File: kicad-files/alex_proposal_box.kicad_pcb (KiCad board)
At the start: 2 copper layers, 69 x 69 mm, 40 parts, among them J1 Conn_01x06_Pin, J2 Conn_01x06_Socket, Q1 2N7000, Q10 2N7000, Q11 2N7000, Q2 2N7000, Q3 2N7000, Q4 2N7000, Q5 2N7000, Q6 2N7000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

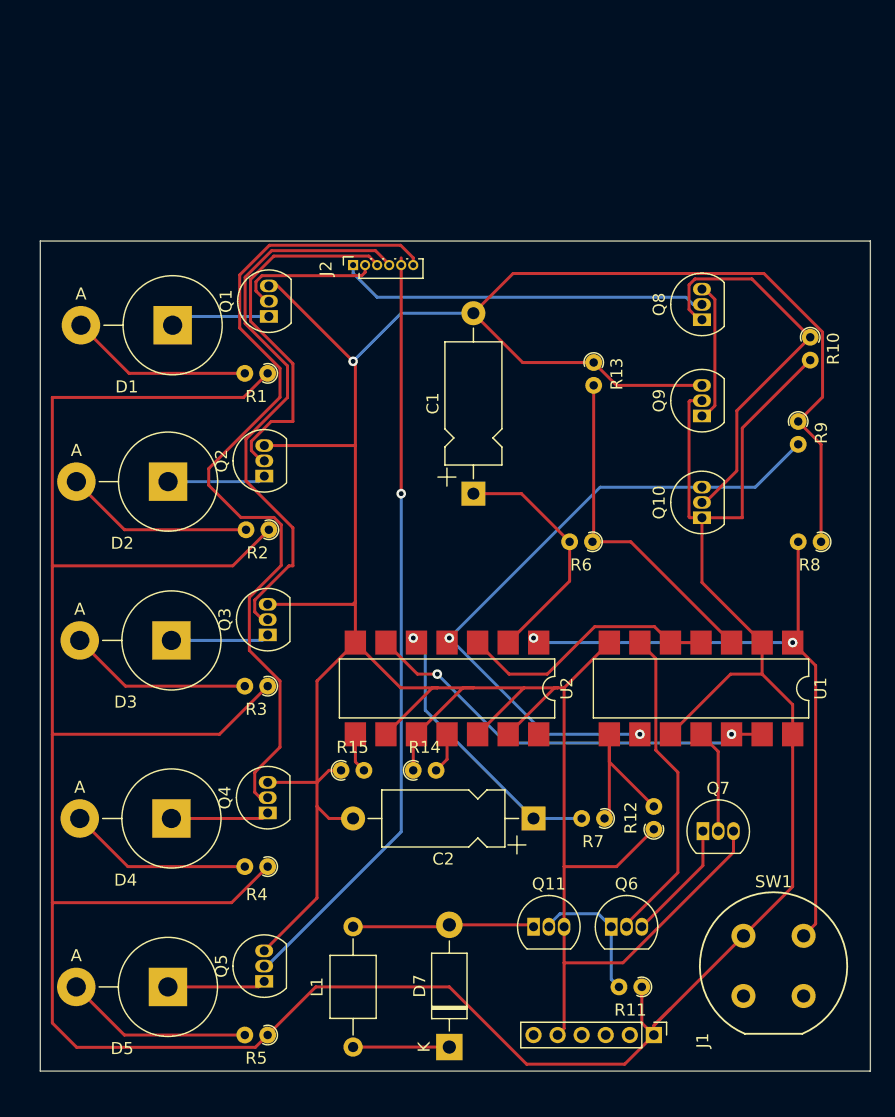
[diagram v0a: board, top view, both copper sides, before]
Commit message: made the schematic printable on a PCB
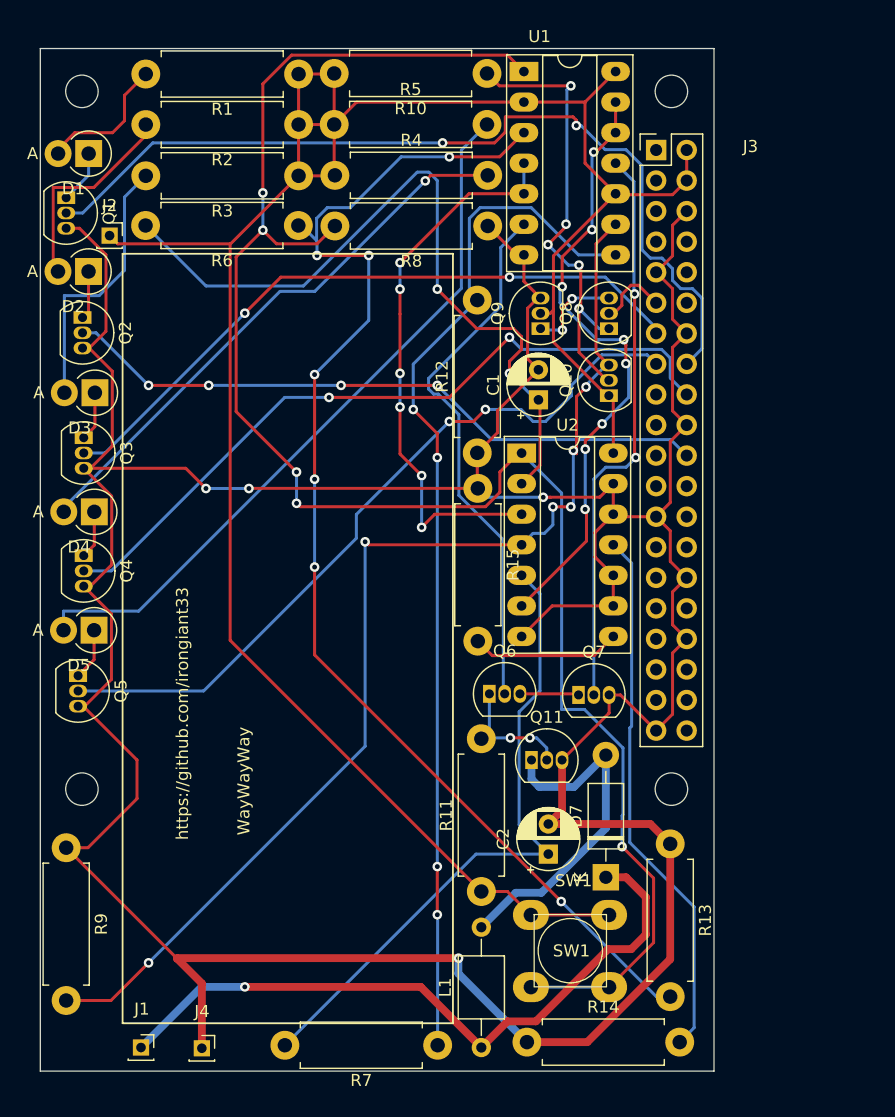
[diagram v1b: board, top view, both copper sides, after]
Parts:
- added J3: Conn_02x20_Odd_Even, Connector_PinHeader_2.54mm:PinHeader_2x20_P2.54mm_Vertical, F.Cu at (143.2, 57.4)
- added J4: Conn_01x01_Socket, Connector_PinSocket_2.00mm:PinSocket_1x01_P2.00mm_Vertical, F.Cu at (105.4, 132.1)
- added REF**: MountingHole_2.7mm, MountingHole:MountingHole_2.7mm, F.Cu at (144.5, 110.6)
- added REF**: MountingHole_2.7mm, MountingHole:MountingHole_2.7mm, F.Cu at (95.5, 52.6)
- added REF**: MountingHole_2.7mm, MountingHole:MountingHole_2.7mm, F.Cu at (144.5, 52.6)
- added REF**: MountingHole_2.7mm, MountingHole:MountingHole_2.7mm, F.Cu at (95.5, 110.6)
- C1, C2: footprint Capacitor_THT:CP_Axial_L10.0mm_D4.5mm_P15.00mm_Horizontal -> Capacitor_THT:CP_Radial_D5.0mm_P2.50mm
- D1, D2, D3, D4, D5: footprint Diode_THT:D_5KPW_P7.62mm_Vertical_AnodeUp -> Diode_THT:D_DO-15_P2.54mm_Vertical_AnodeUp
- J1: value Conn_01x06_Pin -> Conn_01x01_Socket; footprint Connector_PinHeader_2.00mm:PinHeader_1x06_P2.00mm_Vertical -> Connector_PinSocket_2.00mm:PinSocket_1x01_P2.00mm_Vertical
- J2: value Conn_01x06_Socket -> Conn_01x01_Socket; footprint Connector_PinSocket_1.00mm:PinSocket_1x06_P1.00mm_Vertical -> Connector_PinSocket_2.00mm:PinSocket_1x01_P2.00mm_Vertical
- R1, R10, R11, R12, R13, R14, R15, R2, R3, R4, R5, R6, R7, R8, R9: footprint Resistor_THT:R_Axial_DIN0204_L3.6mm_D1.6mm_P1.90mm_Vertical -> Resistor_THT:R_Axial_DIN0411_L9.9mm_D3.6mm_P12.70mm_Horizontal
- SW1: footprint Button_Switch_THT:Push_E-Switch_KS01Q01 -> SamsFootprints:SW_PUSH-6.5mm
- U1, U2: footprint Package_DIP:SMDIP-14_W7.62mm -> Package_DIP:DIP-14_W7.62mm_Socket_LongPads
- moved R5 75.9 mm to (116.4, 55.3), turned to 0 degrees
- moved R9 70.4 mm to (94.2, 115.4)
- moved R4 57.7 mm to (116.5, 59.5), turned to 0 degrees
- moved U1 53.4 mm to (132.2, 50.9), turned to 0 degrees
- moved J1 42.6 mm to (100.4, 132.0), turned to 0 degrees
- moved R3 42.5 mm to (113.5, 59.6)
- moved R13 40.5 mm to (144.4, 115.1)
- moved R8 38.2 mm to (129.2, 63.8)
- moved R6 35.9 mm to (113.5, 63.7)
- moved R10 34.7 mm to (129.1, 51.1), turned to 180 degrees
- moved R12 34.6 mm to (128.3, 82.6)
- moved R2 33.8 mm to (113.5, 55.3)
- moved D5 30.3 mm to (96.5, 97.3)
- moved Q5 29.7 mm to (95.1, 101.1), turned to -90 degrees
- moved Q4 26.3 mm to (95.6, 91.2), turned to -90 degrees
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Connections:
- J1 pad 1: +5VD -> +12V
- J2 pad 1: Net-(J2-Pin_1) -> +5VD
- Q1 pad 2: Net-(J2-Pin_2) -> Net-(J3-Pin_16)
- Q2 pad 2: Net-(J2-Pin_3) -> Net-(J3-Pin_22)
- Q3 pad 2: Net-(J2-Pin_4) -> Net-(J3-Pin_13)
- Q4 pad 2: Net-(J2-Pin_6) -> Net-(J3-Pin_18)
- Q5 pad 2: Net-(J2-Pin_5) -> Net-(J3-Pin_15)
- Q8 pad 2: Net-(J2-Pin_1) -> Net-(J3-Pin_11)
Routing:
- net +5VD: track 283.7 -> 188.1 mm
- net Net-(R8-Pad2): track 55.8 -> 148.0 mm, vias 2 -> 5
- net Net-(R13-Pad2): track 28.1 -> 106.0 mm, vias 0 -> 7
- net Net-(J3-Pin_16): track 0.00 -> 74.1 mm, vias 0 -> 2
- net Net-(J2-Pin_6): track 71.7 -> 0.00 mm
- net Net-(R12-Pad2): track 14.7 -> 86.2 mm, vias 0 -> 4
- net Net-(J2-Pin_5): track 63.7 -> 0.00 mm, vias 1 -> 0
- net Net-(J3-Pin_15): track 0.00 -> 62.4 mm, vias 0 -> 2
- net Net-(J3-Pin_18): track 0.00 -> 61.1 mm, vias 0 -> 2
- net Net-(J3-Pin_13): track 0.00 -> 55.8 mm, vias 0 -> 2
- net Net-(J3-Pin_22): track 0.00 -> 54.4 mm, vias 0 -> 4
- net +12V: track 8.00 -> 57.1 mm, vias 0 -> 1
- net Net-(J2-Pin_4): track 48.6 -> 0.00 mm
- net Net-(D5-A): track 15.7 -> 60.3 mm
- net GND: track 279.5 -> 322.2 mm, vias 1 -> 4
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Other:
- board size 69 x 69 mm -> 56 x 85 mm
- board text added: "WayWayWay"
- board text added: "https://github.com/irongiant33"
